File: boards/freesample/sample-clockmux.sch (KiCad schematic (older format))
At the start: 28 parts, among them J15 SMA, J16 SMA, U11 PI6C59S6005, U12 PI6C59S6005

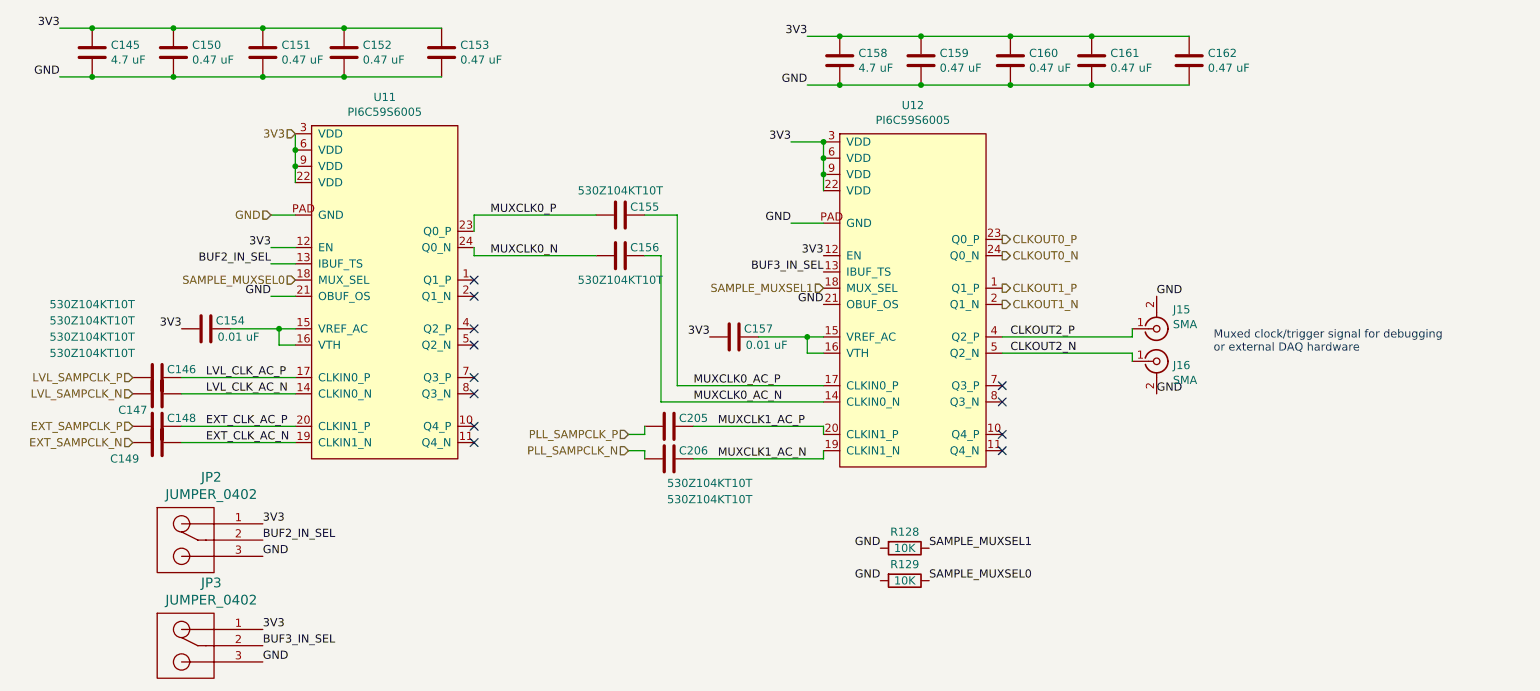
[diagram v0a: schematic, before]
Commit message: Continued layout on clock muxing
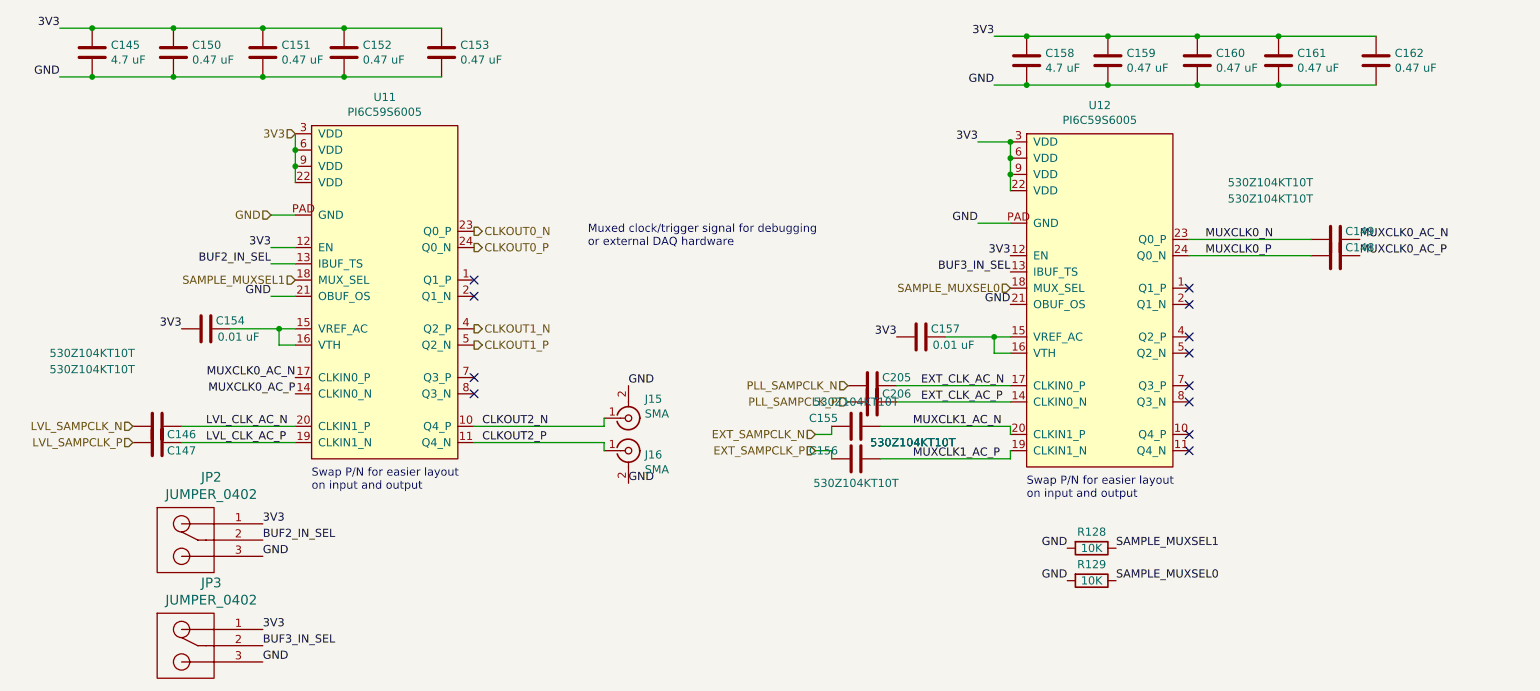
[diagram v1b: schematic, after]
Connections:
- net CLKOUT0_N: now also U11.23 (Q0_P); no longer U12.24 (Q0_N)
- net CLKOUT0_P: now also U11.24 (Q0_N); no longer U12.23 (Q0_P)
- net CLKOUT1_N: now also U11.4 (Q2_P); no longer U12.2 (Q1_N)
- net CLKOUT1_P: now also U11.5 (Q2_N); no longer U12.1 (Q1_P)
- net CLKOUT2_N: now also J15.1 (In), U11.10 (Q4_P); no longer J16.1 (In), U12.5 (Q2_N)
- net CLKOUT2_P: now also J16.1 (In), U11.11 (Q4_N); no longer J15.1 (In), U12.4 (Q2_P)
- net EXT_CLK_AC_N: now also C205.1, U12.17 (CLKIN0_P); no longer C149.1, U11.19 (CLKIN1_N)
- net EXT_CLK_AC_P: now also C206.1, U12.14 (CLKIN0_N); no longer C148.1, U11.20 (CLKIN1_P)
- net EXT_SAMPCLK_N: now also C155.2; no longer C149.2
- net EXT_SAMPCLK_P: now also C156.2; no longer C148.2
- net LVL_CLK_AC_N: now also U11.20 (CLKIN1_P); no longer U11.14 (CLKIN0_N)
- net LVL_CLK_AC_P: now also U11.19 (CLKIN1_N); no longer U11.17 (CLKIN0_P)
- net MUXCLK0_AC_N: now also C149.1, U11.17 (CLKIN0_P); no longer C156.1, U12.14 (CLKIN0_N)
- net MUXCLK0_AC_P: now also C148.1, U11.14 (CLKIN0_N); no longer C155.1, U12.17 (CLKIN0_P)
- net MUXCLK0_N: now also C149.2, U12.23 (Q0_P); no longer C156.2, U11.24 (Q0_N)
- net MUXCLK0_P: now also C148.2, U12.24 (Q0_N); no longer C155.2, U11.23 (Q0_P)
- net MUXCLK1_AC_N: now also C155.1, U12.20 (CLKIN1_P); no longer C206.1, U12.19 (CLKIN1_N)
- net MUXCLK1_AC_P: now also C156.1, U12.19 (CLKIN1_N); no longer C205.1, U12.20 (CLKIN1_P)
- net PLL_SAMPCLK_N: now also C205.2; no longer C206.2
- net PLL_SAMPCLK_P: now also C206.2; no longer C205.2
- net SAMPLE_MUXSEL0: now also U12.18 (MUX_SEL); no longer U11.18 (MUX_SEL)
- net SAMPLE_MUXSEL1: now also U11.18 (MUX_SEL); no longer U12.18 (MUX_SEL)
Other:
- note added: "Swap P/N for easier layout\non input and output"
- moved on the sheet: C146, C147, C148, C149, C155, C156, C157, C158, C159, C160, C161, C162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

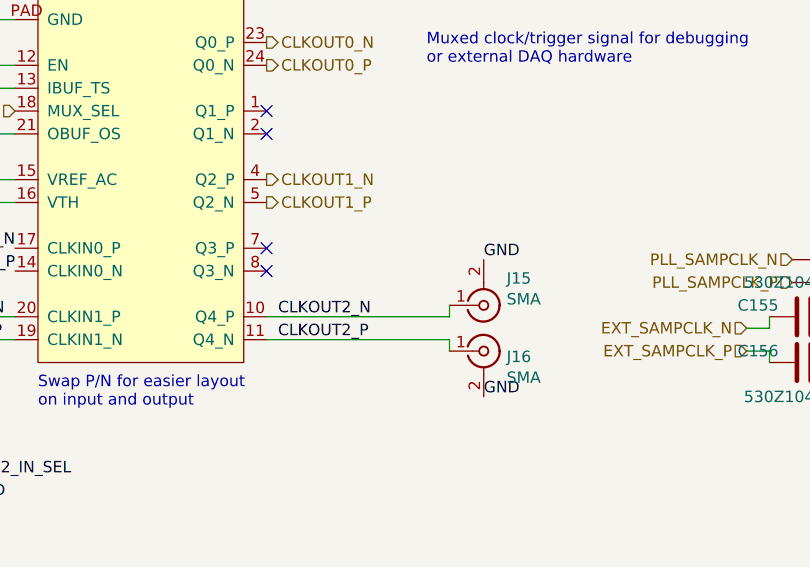
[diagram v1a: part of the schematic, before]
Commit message: Initial layout of coarse delay line
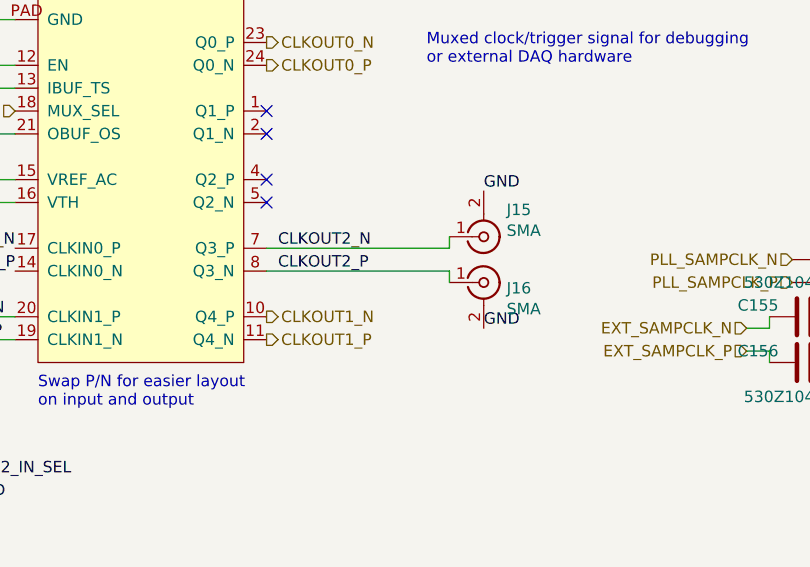
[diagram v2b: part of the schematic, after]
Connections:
- net CLKOUT1_N: now also U11.10 (Q4_P); no longer U11.4 (Q2_P)
- net CLKOUT1_P: now also U11.11 (Q4_N); no longer U11.5 (Q2_N)
- net CLKOUT2_N: now also U11.7 (Q3_P); no longer U11.10 (Q4_P)
- net CLKOUT2_P: now also U11.8 (Q3_N); no longer U11.11 (Q4_N)
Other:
- moved on the sheet: J15, J16
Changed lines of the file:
@@
 Sheet 11 12
 Title "FREESAMPLE Oscilloscope"
-Date "2019-03-24"
+Date "2019-03-25"
 Rev "0.1"
 Comp "Andrew D. Zonenberg / Antikernel Labs"
 Comment1 "Sample clock muxing"
-Comment2 "Initial layout in progress"
+Comment2 "Initial layout complete"
 Comment3 ""
 Comment4 ""
@@
 Text HLabel 3450 1900 2    50   Output ~ 0
 CLKOUT0_N
-Text HLabel 3450 2600 2    50   Output ~ 0
+Text HLabel 3450 3200 2    50   Output ~ 0
 CLKOUT1_P
-Text HLabel 3450 2500 2    50   Output ~ 0
+Text HLabel 3450 3100 2    50   Output ~ 0
 CLKOUT1_N
 Text HLabel 2350 1300 0    50   Input ~ 0
@@
 NoConn ~ 7850 3150
 NoConn ~ 7850 3250
-NoConn ~ 3450 2800
-NoConn ~ 3450 2900
 Text Label 2350 2900 2    50   ~ 0
 MUXCLK0_AC_P
@@
 L Connector:Conn_Coaxial J16
 U 1 1 5D26866A
-P 4400 3250
-F 0 "J16" H 4500 3225 50  0000 L CNN
-F 1 "SMA" H 4500 3134 50  0000 L CNN
-F 2 "azonenberg_pcb:CONN_SMA_EDGE_SAMTEC_SMA_J_P_H_ST_EM1" H 4400 3250 50  0001 C CNN
-F 3 "" H 4400 3250 50  0001 C CNN
-	1    4400 3250
+P 4400 2950
+F 0 "J16" H 4500 2925 50  0000 L CNN
+F 1 "SMA" H 4500 2834 50  0000 L CNN
+F 2 "azonenberg_pcb:CONN_SMA_EDGE_SAMTEC_SMA_J_P_H_ST_EM1" H 4400 2950 50  0001 C CNN
+F 3 "" H 4400 2950 50  0001 C CNN
+	1    4400 2950
 	1    0    0    -1
 $EndComp
@@
 L Connector:Conn_Coaxial J15
 U 1 1 5D268D26
-P 4400 3050
-F 0 "J15" H 4500 2932 50  0000 L CNN
-F 1 "SMA" H 4500 3023 50  0000 L CNN
-F 2 "azonenberg_pcb:CONN_SMA_EDGE_SAMTEC_SMA_J_P_H_ST_EM1" H 4400 3050 50  0001 C CNN
-F 3 "" H 4400 3050 50  0001 C CNN
-	1    4400 3050
+P 4400 2750
+F 0 "J15" H 4500 2632 50  0000 L CNN
+F 1 "SMA" H 4500 2723 50  0000 L CNN
+F 2 "azonenberg_pcb:CONN_SMA_EDGE_SAMTEC_SMA_J_P_H_ST_EM1" H 4400 2750 50  0001 C CNN
+F 3 "" H 4400 2750 50  0001 C CNN
+	1    4400 2750
 	1    0    0    1
 $EndComp
 Wire Wire Line
-	3450 3100 4250 3100
-Wire Wire Line
-	4250 3100 4250 3050
-Wire Wire Line
-	3450 3200 4250 3200
-Wire Wire Line
-	4250 3200 4250 3250
-Text Label 4400 2850 0    50   ~ 0
-GND
-Text Label 4400 3450 0    50   ~ 0
-GND
-Text Label 3500 3200 0    50   ~ 0
+	3450 2800 4250 2800
+Wire Wire Line
+	4250 2800 4250 2750
+Wire Wire Line
+	3450 2900 4250 2900
+Wire Wire Line
+	4250 2900 4250 2950
+Text Label 4400 2550 0    50   ~ 0
+GND
+Text Label 4400 3150 0    50   ~ 0
+GND
+Text Label 3500 2900 0    50   ~ 0
 CLKOUT2_P
-Text Label 3500 3100 0    50   ~ 0
+Text Label 3500 2800 0    50   ~ 0
 CLKOUT2_N
 Text Notes 4150 2000 0    50   ~ 0
@@
 Text Notes 6850 3550 0    50   ~ 0
 Swap P/N for easier layout\non input and output
+NoConn ~ 3450 2500
+NoConn ~ 3450 2600
 $EndSCHEMATC

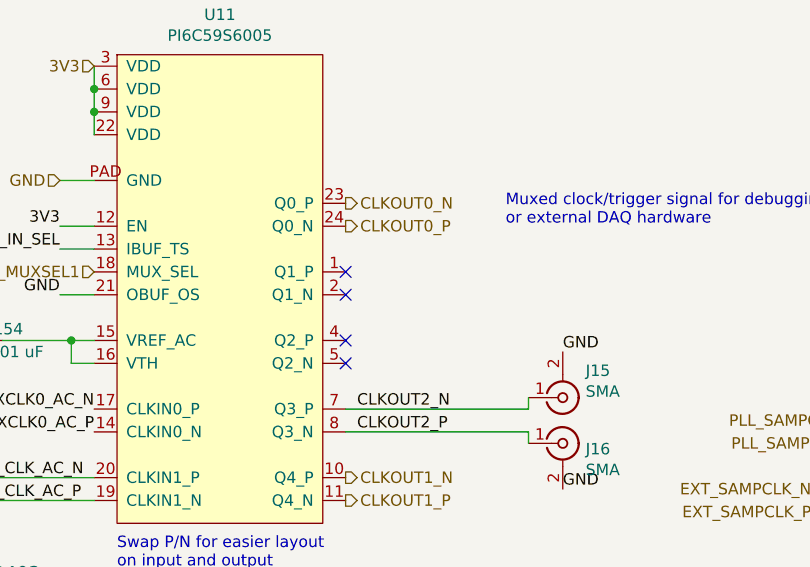
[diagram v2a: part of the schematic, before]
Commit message: Finished initial layout of delay lines
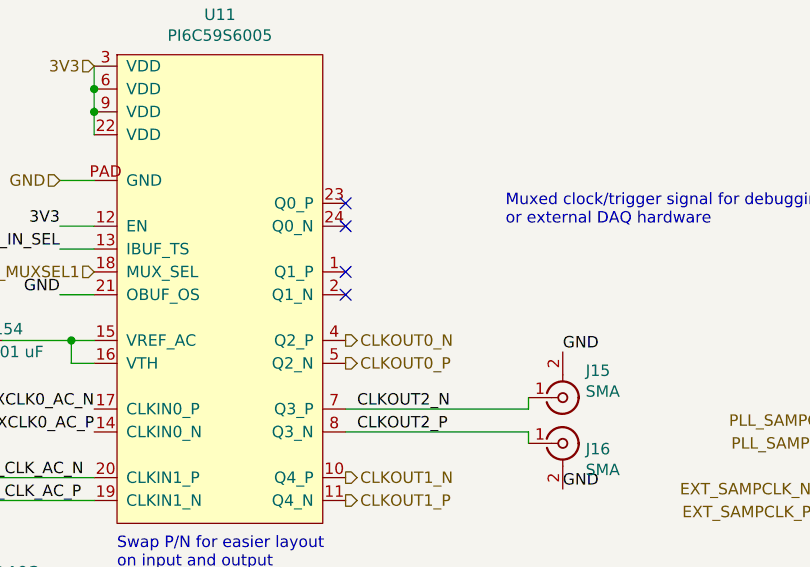
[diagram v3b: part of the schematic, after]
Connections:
- net CLKOUT0_N: now also U11.4 (Q2_P); no longer U11.23 (Q0_P)
- net CLKOUT0_P: now also U11.5 (Q2_N); no longer U11.24 (Q0_N)
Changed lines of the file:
@@
 Sheet 11 12
 Title "FREESAMPLE Oscilloscope"
-Date "2019-03-25"
+Date "2019-03-28"
 Rev "0.1"
 Comp "Andrew D. Zonenberg / Antikernel Labs"
@@
 	1    0    0    -1
 $EndComp
-Text HLabel 3450 2000 2    50   Output ~ 0
+Text HLabel 3450 2600 2    50   Output ~ 0
 CLKOUT0_P
-Text HLabel 3450 1900 2    50   Output ~ 0
+Text HLabel 3450 2500 2    50   Output ~ 0
 CLKOUT0_N
 Text HLabel 3450 3200 2    50   Output ~ 0
@@
 Text Notes 6850 3550 0    50   ~ 0
 Swap P/N for easier layout\non input and output
-NoConn ~ 3450 2500
-NoConn ~ 3450 2600
+NoConn ~ 3450 2000
+NoConn ~ 3450 1900
 $EndSCHEMATC
